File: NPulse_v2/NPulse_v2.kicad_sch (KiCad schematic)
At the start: 20 parts, among them J2 Conn_01x04_Pin, SW1 SW_Push, SW2 SW_SPDT, U5 STM32G484METx, Y1 16MHz

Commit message: Add MCU, FSR, motor drivers, light sensing
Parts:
- added C110, C113: 100nF, symbol Device:C
- added C99: 100nF, Capacitor_SMD:C_0402_1005Metric, symbol Device:C
- added D1: LED, symbol Device:LED
- added IC1: TXU0202QDCURQ1, SOP50P310X90-8N, symbol TXU0202QDCURQ1:TXU0202QDCURQ1
- added J21: Conn_01x04_Pin, symbol Connector:Conn_01x04_Pin
- added R57: 1M, symbol Device:R
- renumbered C26 to C12, C27 to C13, U5 to U1
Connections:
- net +3.3V: now also C110.2, IC1.3 (VCCA)
- net GND: now also C110.1, C113.1, C99.2, D1.1 (K), IC1.2 (GND), J21.4 (Pin_4), R57.2
- net NSS: now reaches U1.18 (PA4)
- net SCK: now reaches U1.19 (PA5)
- net MISO: now reaches U1.20 (PA6)
- net MOSI: now reaches U1.21 (PA7)
- net TX: now reaches U1.66 (PC10)
- net TX: now also IC1.5 (A1)
- net RX: now reaches U1.67 (PC11)
- net RX: now also IC1.4 (A2Y)
- new net: C113.2, IC1.7 (VCCB), J21.1 (Pin_1)
- new net: IC1.8 (B1Y), J21.2 (Pin_2)
- new net: IC1.1 (B2), J21.3 (Pin_3)
- new net LED: C99.1, D1.2 (A), R57.1
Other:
- added sheet COM_EMG (COM_EMG.kicad_sch)
- added sheet FSR (FSR.kicad_sch)
- added sheet motor_driver2 (motor_driver2.kicad_sch)
- added sheet test (test.kicad_sch)
- note added: "- change footprint of 74LVC - place DIR, I, FSR pins - connection with emg board - connection with supply board - encoder sensors"
- note added: "Microcontroller"
- note added: "RS485 with the EMG board"
- note added: "TIM2 (32 bits): CH1 (PA0, PA5, PA15), CH2 (PA1, PB3), CH3 (PA2, PA9, PB10), CH4 (PA3, PA10, PB11) (max 4) TIM5 (32 bits) : CH1 (PA0, PB2), CH2 (PA1, PC12), CH3 (PA2, PE8), CH4 (PA3, PE9) (max 4) TIM3 (16 bits) TIM4 (16 bits)"
- note added: "TIMER 1 : PC0, PC1, PC2, PC3, PA8, PA9, PA10, PA11 (max 4) TIMER 8 : PB6, PB7, PB8, PB9, PC6, PC7, PC8, PC9 (max 4)"
- note added: "Tasks:"
- note added: "Timers for encoders"
- note added: "Timers for motors control"
- note added: "UART Protocol"
- note added: "input"
- note removed: "TIMER 1 : PC0, PC1, PC2, PC3, PA8, PA9, PA10, PA11 (max 4) TIMER 8 : PB6, PB7, PB8, PB9, PC6, PC7, PC8, PC9 (max 4) TIMER 20 : PB2, PC2, PC8 (max 4)"
- moved on the sheet: C1, C10, C11, C12, C13, C2, C3, C4, C5, C6, C7, C8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

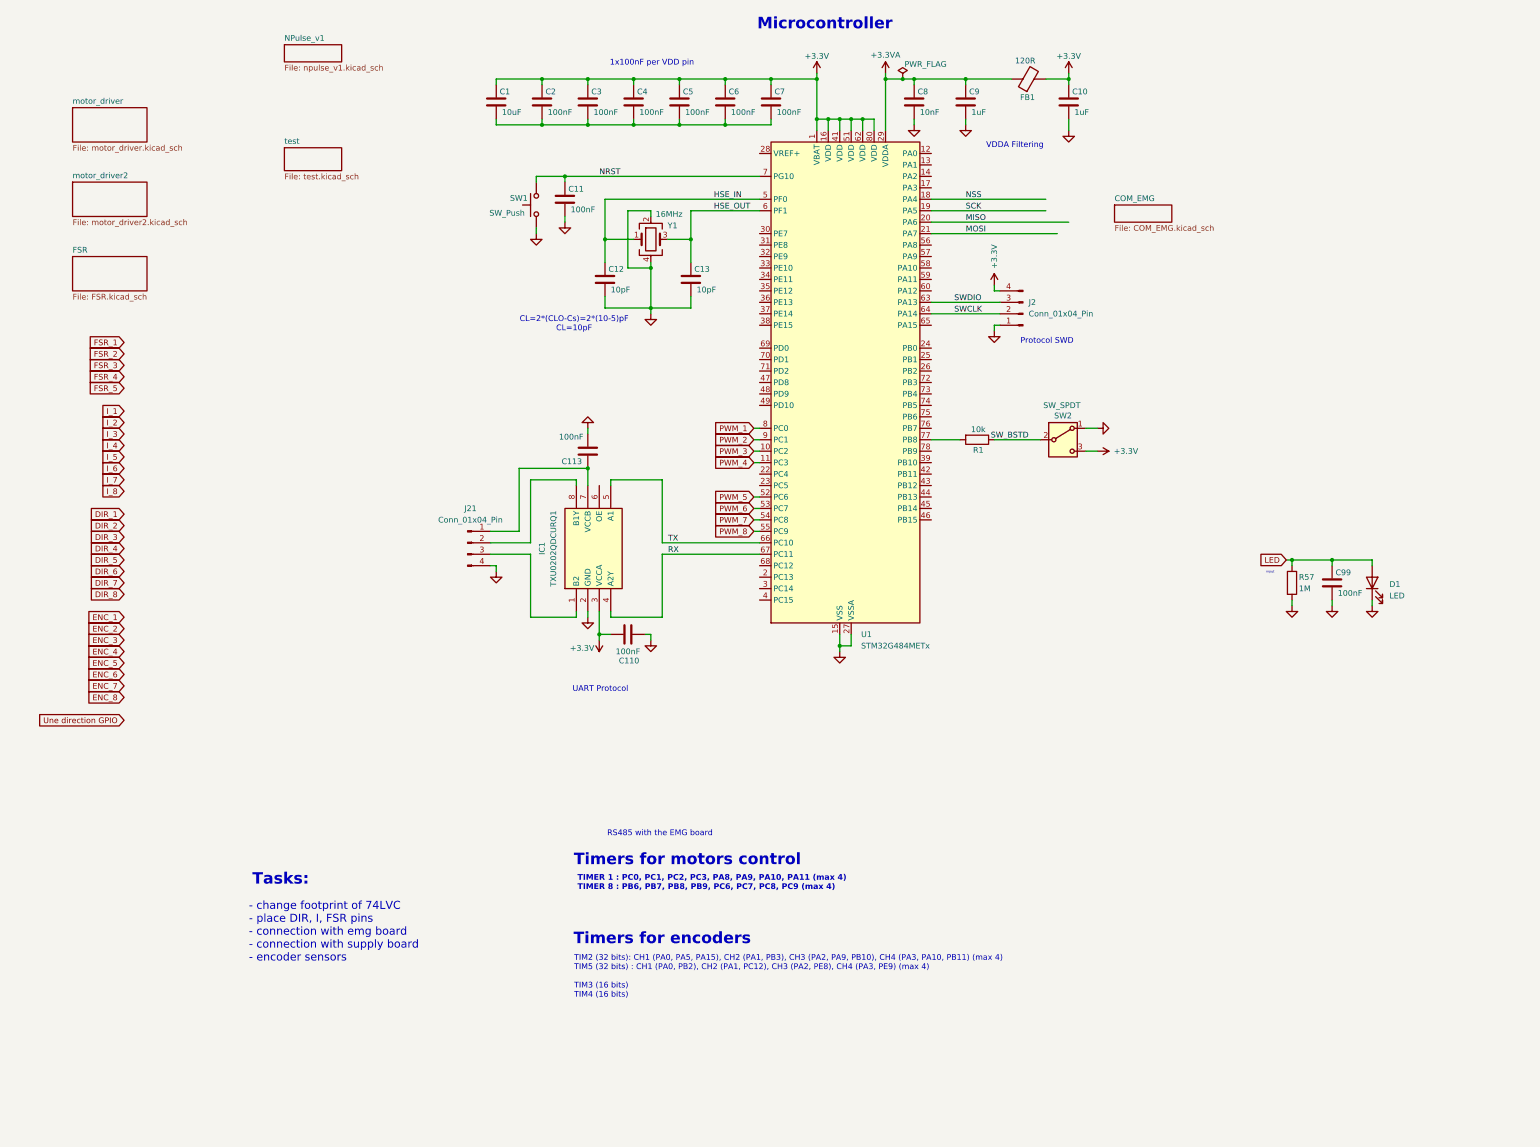
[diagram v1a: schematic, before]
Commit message: Version 3 - motor driver updated, FSR updated
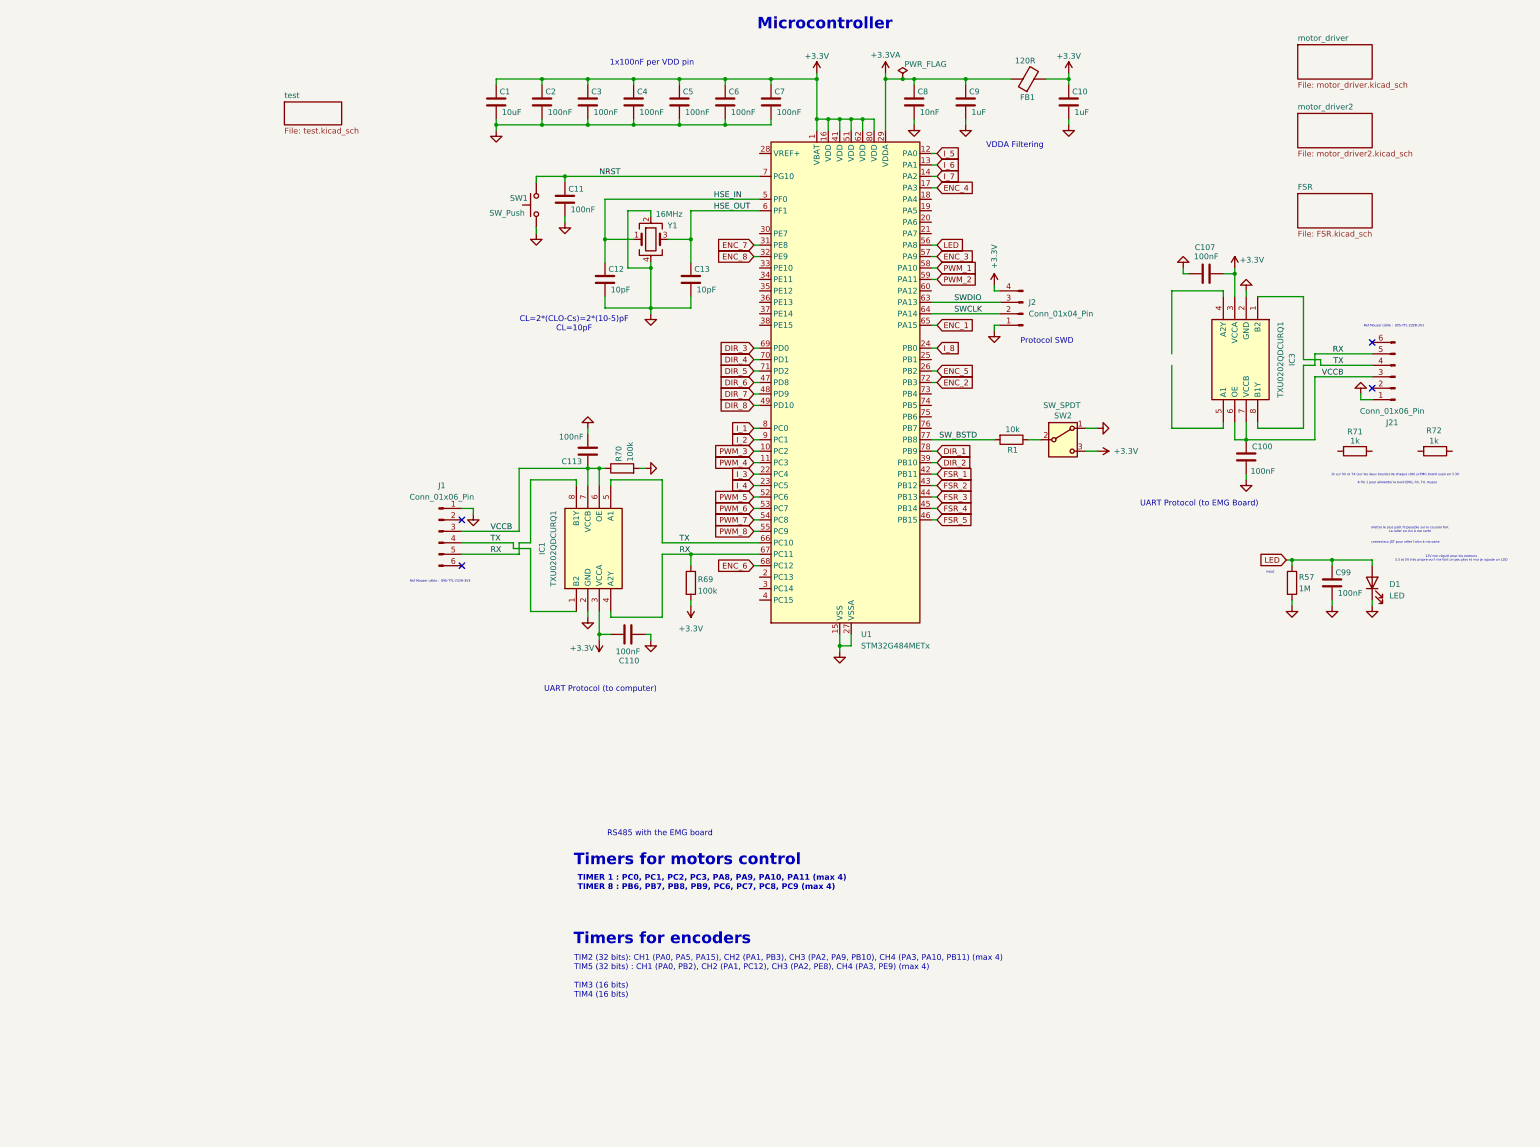
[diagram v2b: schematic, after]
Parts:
- removed J21: Conn_01x04_Pin, symbol Connector:Conn_01x04_Pin
- added C100, C107: 100nF, symbol Device:C
- added IC3: TXU0202QDCURQ1, symbol TXU0202QDCURQ1:TXU0202QDCURQ1
- added J1, J21: Conn_01x06_Pin, symbol Connector:Conn_01x06_Pin
- added R69, R70: 100k, symbol Device:R
- added R71, R72: 1k, symbol Device:R
- C1: footprint Capacitor_SMD:C_0603_1608Metric -> (none)
- C10, C11, C12, C13, C2, C3, C4, C5, C6, C7, C8, C9, C99: footprint Capacitor_SMD:C_0402_1005Metric -> (none)
- FB1: footprint Inductor_SMD:L_0603_1608Metric -> (none)
- IC1: footprint SOP50P310X90-8N -> (none)
- J2: footprint Connector_PinHeader_2.54mm:PinHeader_1x04_P2.54mm_Vertical -> (none)
- R1: footprint Resistor_SMD:R_0402_1005Metric -> (none)
- SW2: footprint Button_Switch_SMD:SW_SPDT_PCM12 -> (none)
- U1: footprint Package_QFP:LQFP-80_12x12mm_P0.5mm -> (none)
- Y1: footprint Crystal:Crystal_SMD_3225-4Pin_3.2x2.5mm -> (none)
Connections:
- net +3.3V: now also C107.2, IC3.3 (VCCA), R69.2
- net DIR_1: now also U1.78 (PB9)
- net DIR_2: now also U1.39 (PB10)
- net DIR_3: now also U1.69 (PD0)
- net DIR_4: now also U1.70 (PD1)
- net DIR_5: now also U1.71 (PD2)
- net DIR_6: now also U1.47 (PD8)
- net DIR_7: now also U1.48 (PD9)
- net DIR_8: now also U1.49 (PD10)
- net ENC_1: now also U1.65 (PA15)
- net ENC_2: now also U1.72 (PB3)
- net ENC_3: now also U1.57 (PA9)
- net ENC_4: now also U1.17 (PA3)
- net ENC_5: now also U1.26 (PB2)
- net ENC_6: now also U1.68 (PC12)
- net ENC_7: now also U1.31 (PE8)
- net ENC_8: now also U1.32 (PE9)
- net FSR_1: now also U1.42 (PB11)
- net FSR_2: now also U1.43 (PB12)
- net FSR_3: now also U1.44 (PB13)
- net FSR_4: now also U1.45 (PB14)
- net FSR_5: now also U1.46 (PB15)
- net GND: now also C1.2, C2.2, C3.2, C4.2, C5.2, C6.2, C7.2, C100.1, C107.1, IC3.2 (GND), J1.1 (Pin_1), J21.1 (Pin_1), R70.2
- net I_1: now also U1.8 (PC0)
- net I_2: now also U1.9 (PC1)
- net I_3: now also U1.22 (PC4)
- net I_4: now also U1.23 (PC5)
- net I_5: now also U1.12 (PA0)
- net I_6: now also U1.13 (PA1)
- net I_7: now also U1.14 (PA2)
- net I_8: now also U1.24 (PB0)
- net LED: now also U1.56 (PA8)
- net PWM_1: now also U1.58 (PA10); no longer U1.8 (PC0)
- net PWM_2: now also U1.59 (PA11); no longer U1.9 (PC1)
- net RX: now also IC1.8 (B1Y), IC3.8 (B1Y), J1.5 (Pin_5), J21.5 (Pin_5), R69.1
- net SW_BSTD: now also R1.2, U1.77 (PB8); no longer R1.1, SW2.2 (B)
- net TX: now also IC1.1 (B2), IC3.1 (B2), J1.4 (Pin_4), J21.4 (Pin_4)
- net VCCB: now reaches C113.2, IC1.7 (VCCB)
- net VCCB: now also IC1.6 (OE), C100.2, IC3.6 (OE), IC3.7 (VCCB), J1.3 (Pin_3), J21.3 (Pin_3), R70.1
- net MISO: no longer names the net of U1.20 (PA6)
- net MOSI: no longer names the net of U1.21 (PA7)
- net NSS: no longer names the net of U1.18 (PA4)
- net SCK: no longer names the net of U1.19 (PA5)
- new net: R1.1, SW2.2 (B)
- no-connect marks 0 -> 4
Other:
- removed sheet COM_EMG
- removed sheet NPulse_v1
- note added: "12V non régulé pour les moteurs 3.3 et 5V très propre ou il me font un peu plus et moi je rajoute un LDO"
- note added: "1k sur RX et TX (sur les deux boards) de chaque côté si EMG board aussi en 3.3V"
- note added: "4 fils 1 pour alimenter la bord EMG, RX, TX, masse"
- note added: "Ref Mouser câble : 895-TTL-232R-3V3"
- note added: "UART Protocol (to EMG Board)"
- note added: "UART Protocol (to computer)"
- note added: "connecteur JST pour relier l'alim à ma carte"
- note added: "mettre le plus petit fil possible sur le courant fort La relier en dur à ma carte"
- note removed: "- change footprint of 74LVC - place DIR, I, FSR pins - connection with emg board - connection with supply board - encoder sensors"
- note removed: "Tasks:"
- note removed: "UART Protocol"
- moved on the sheet: R1
